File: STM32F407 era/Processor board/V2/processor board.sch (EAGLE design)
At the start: 43 parts, among them IC1 REG1117, U2 MAX13052ESA+, X1 MINI-USB-SCHIELD-32005-201, X2 057-010-1, Y1 25 MHz, Y2 32.768KHz

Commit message: minor updates to board layout
Added USB power fuse, and added toggle switch for boot switch
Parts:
- removed S2: BOOT, SparkFun-Electromechanical:SWITCH-MOMENTARY-2SMD-1101NE
- added U$32: SWITCH_SPDT, SparkFun-Electromechanical:SWITCH_SPDT
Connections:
- new net N$7: C17.P$2, IC1.VIN, PTC1.1
- net 3.3V: now also U$32.O; no longer S2.2
- net N$4: now also U$32.P; no longer S2.1
- net USB_VBUS: now also PTC1.2; no longer C17.P$2, IC1.VIN
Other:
- moved on the sheet: C17, C18, IC1, LED1, PTC1, R3
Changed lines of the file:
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@@
 <part name="U$6" library="microbuilder" deviceset="3.3V" device=""/>
 <part name="S1" library="SparkFun-Electromechanical" deviceset="SWITCH-MOMENTARY-2" device="SMD-1101NE" value="RESET"/>
-<part name="S2" library="SparkFun-Electromechanical" deviceset="SWITCH-MOMENTARY-2" device="SMD-1101NE" value="BOOT"/>
 <part name="R1" library="microbuilder" deviceset="RESISTOR" device="_0603MP" value="500"/>
 <part name="U$7" library="microbuilder" deviceset="3.3V" device=""/>
@@
 <part name="U$12" library="microbuilder" deviceset="GND" device=""/>
 <part name="PTC1" library="microbuilder" deviceset="PTC" device="1206"/>
+<part name="U$32" library="SparkFun-Electromechanical" deviceset="SWITCH_SPDT" device=""/>
 </parts>
 <sheets>
@@
 <instance part="U$6" gate="G$1" x="17.78" y="53.34"/>
 <instance part="S1" gate="G$1" x="162.56" y="10.16"/>
-<instance part="S2" gate="G$1" x="182.88" y="7.62"/>
 <instance part="R1" gate="G$1" x="175.26" y="0" rot="R270"/>
-<instance part="U$7" gate="G$1" x="190.5" y="12.7"/>
+<instance part="U$7" gate="G$1" x="187.96" y="15.24"/>
 <instance part="U$8" gate="G$1" x="175.26" y="-7.62"/>
 <instance part="R2" gate="G$1" x="152.4" y="17.78" rot="R270"/>
@@
 <instance part="BAT1" gate="G$1" x="30.48" y="53.34"/>
 <instance part="U$18" gate="G$1" x="38.1" y="48.26"/>
-<instance part="IC1" gate="G$1" x="251.46" y="104.14"/>
-<instance part="U$19" gate="G$1" x="266.7" y="109.22"/>
-<instance part="U$20" gate="G$1" x="251.46" y="83.82"/>
-<instance part="C17" gate="G$1" x="236.22" y="96.52" rot="R180"/>
-<instance part="C18" gate="G$1" x="266.7" y="96.52"/>
+<instance part="IC1" gate="G$1" x="261.62" y="104.14"/>
+<instance part="U$19" gate="G$1" x="276.86" y="109.22"/>
+<instance part="U$20" gate="G$1" x="261.62" y="83.82"/>
+<instance part="C17" gate="G$1" x="246.38" y="96.52" rot="R180"/>
+<instance part="C18" gate="G$1" x="276.86" y="96.52"/>
 <instance part="U2" gate="A" x="226.06" y="0" smashed="yes">
 <attribute name="NAME" x="221.3356" y="14.1986" size="2.0828" layer="95" ratio="10" rot="SR0"/>
@@
 <instance part="U$30" gate="G$1" x="304.8" y="35.56" rot="MR0"/>
 <instance part="TP1" gate="G$1" x="165.1" y="50.8"/>
-<instance part="LED1" gate="G$1" x="284.48" y="104.14" rot="R90"/>
-<instance part="R3" gate="G$1" x="274.32" y="104.14"/>
-<instance part="U$31" gate="G$1" x="292.1" y="99.06" rot="MR0"/>
+<instance part="LED1" gate="G$1" x="294.64" y="104.14" rot="R90"/>
+<instance part="R3" gate="G$1" x="284.48" y="104.14"/>
+<instance part="U$31" gate="G$1" x="302.26" y="99.06" rot="MR0"/>
 <instance part="JP6" gate="G$1" x="38.1" y="68.58" rot="R180"/>
 <instance part="U$11" gate="G$1" x="215.9" y="25.4" rot="MR0"/>
 <instance part="U$12" gate="G$1" x="203.2" y="25.4" rot="MR0"/>
-<instance part="PTC1" gate="G$1" x="144.78" y="121.92"/>
+<instance part="PTC1" gate="G$1" x="238.76" y="104.14"/>
+<instance part="U$32" gate="G$1" x="180.34" y="7.62"/>
 </instances>
 <busses>
@@
 <pinref part="IC1" gate="G$1" pin="GND"/>
 <pinref part="U$20" gate="G$1" pin="GND"/>
-<wire x1="251.46" y1="86.36" x2="251.46" y2="88.9" width="0.1524" layer="91"/>
+<wire x1="261.62" y1="86.36" x2="261.62" y2="88.9" width="0.1524" layer="91"/>
 <pinref part="C17" gate="G$1" pin="P$1"/>
-<wire x1="251.46" y1="88.9" x2="251.46" y2="91.44" width="0.1524" layer="91"/>
-<wire x1="236.22" y1="91.44" x2="236.22" y2="88.9" width="0.1524" layer="91"/>
-<wire x1="236.22" y1="88.9" x2="251.46" y2="88.9" width="0.1524" layer="91"/>
-<junction x="251.46" y="88.9"/>
+<wire x1="261.62" y1="88.9" x2="261.62" y2="91.44" width="0.1524" layer="91"/>
+<wire x1="246.38" y1="91.44" x2="246.38" y2="88.9" width="0.1524" layer="91"/>
+<wire x1="246.38" y1="88.9" x2="261.62" y2="88.9" width="0.1524" layer="91"/>
+<junction x="261.62" y="88.9"/>
 <pinref part="C18" gate="G$1" pin="P$2"/>
-<wire x1="251.46" y1="88.9" x2="266.7" y2="88.9" width="0.1524" layer="91"/>
-<wire x1="266.7" y1="88.9" x2="266.7" y2="93.98" width="0.1524" layer="91"/>
+<wire x1="261.62" y1="88.9" x2="276.86" y2="88.9" width="0.1524" layer="91"/>
+<wire x1="276.86" y1="88.9" x2="276.86" y2="93.98" width="0.1524" layer="91"/>
 </segment>
 <segment>
@@
 <pinref part="LED1" gate="G$1" pin="C"/>
 <pinref part="U$31" gate="G$1" pin="GND"/>
-<wire x1="289.56" y1="104.14" x2="292.1" y2="104.14" width="0.1524" layer="91"/>
-<wire x1="292.1" y1="104.14" x2="292.1" y2="101.6" width="0.1524" layer="91"/>
+<wire x1="299.72" y1="104.14" x2="302.26" y2="104.14" width="0.1524" layer="91"/>
+<wire x1="302.26" y1="104.14" x2="302.26" y2="101.6" width="0.1524" layer="91"/>
 </segment>
 <segment>
@@
 </segment>
 <segment>
-<pinref part="S2" gate="G$1" pin="2"/>
 <pinref part="U$7" gate="G$1" pin="3.3V"/>
-<wire x1="187.96" y1="7.62" x2="190.5" y2="7.62" width="0.1524" layer="91"/>
-<wire x1="190.5" y1="7.62" x2="190.5" y2="10.16" width="0.1524" layer="91"/>
+<wire x1="185.42" y1="10.16" x2="187.96" y2="10.16" width="0.1524" layer="91"/>
+<wire x1="187.96" y1="10.16" x2="187.96" y2="12.7" width="0.1524" layer="91"/>
+<pinref part="U$32" gate="G$1" pin="O"/>
 </segment>
 <segment>
@@
 <pinref part="IC1" gate="G$1" pin="VOUT"/>
 <pinref part="U$19" gate="G$1" pin="3.3V"/>
-<wire x1="264.16" y1="104.14" x2="266.7" y2="104.14" width="0.1524" layer="91"/>
-<wire x1="266.7" y1="104.14" x2="266.7" y2="106.68" width="0.1524" layer="91"/>
+<wire x1="274.32" y1="104.14" x2="276.86" y2="104.14" width="0.1524" layer="91"/>
+<wire x1="276.86" y1="104.14" x2="276.86" y2="106.68" width="0.1524" layer="91"/>
 <pinref part="C18" gate="G$1" pin="P$1"/>
-<wire x1="266.7" y1="104.14" x2="266.7" y2="101.6" width="0.1524" layer="91"/>
-<junction x="266.7" y="104.14"/>
+<wire x1="276.86" y1="104.14" x2="276.86" y2="101.6" width="0.1524" layer="91"/>
+<junction x="276.86" y="104.14"/>
 <pinref part="R3" gate="G$1" pin="1"/>
-<wire x1="266.7" y1="104.14" x2="269.24" y2="104.14" width="0.1524" layer="91"/>
+<wire x1="276.86" y1="104.14" x2="279.4" y2="104.14" width="0.1524" layer="91"/>
 </segment>
 <segment>
@@
 <segment>
 <pinref part="U1" gate="G$7" pin="BOOT0"/>
-<pinref part="S2" gate="G$1" pin="1"/>
 <wire x1="149.86" y1="7.62" x2="175.26" y2="7.62" width="0.1524" layer="91"/>
 <pinref part="R1" gate="G$1" pin="1"/>
@@
 <wire x1="175.26" y1="7.62" x2="175.26" y2="5.08" width="0.1524" layer="91"/>
 <junction x="175.26" y="7.62"/>
+<pinref part="U$32" gate="G$1" pin="P"/>
 </segment>
 </net>
@@
 <pinref part="C16" gate="G$1" pin="P$1"/>
 <wire x1="213.36" y1="104.14" x2="228.6" y2="104.14" width="0.1524" layer="91"/>
-<pinref part="IC1" gate="G$1" pin="VIN"/>
-<wire x1="228.6" y1="104.14" x2="236.22" y2="104.14" width="0.1524" layer="91"/>
+<pinref part="PTC1" gate="G$1" pin="2"/>
+<wire x1="228.6" y1="104.14" x2="233.68" y2="104.14" width="0.1524" layer="91"/>
 <junction x="228.6" y="104.14"/>
-<pinref part="C17" gate="G$1" pin="P$2"/>
-<wire x1="236.22" y1="104.14" x2="238.76" y2="104.14" width="0.1524" layer="91"/>
-<wire x1="236.22" y1="104.14" x2="236.22" y2="99.06" width="0.1524" layer="91"/>
-<junction x="236.22" y="104.14"/>
 </segment>
 </net>
@@
 <pinref part="R3" gate="G$1" pin="2"/>
 <pinref part="LED1" gate="G$1" pin="A"/>
-<wire x1="281.94" y1="104.14" x2="279.4" y2="104.14" width="0.1524" layer="91"/>
-</segment>
-</net>
+<wire x1="292.1" y1="104.14" x2="289.56" y2="104.14" width="0.1524" layer="91"/>
+</segment>
+</net>
+<net name="N$7" class="0">
+<segment>
+<pinref part="C17" gate="G$1" pin="P$2"/>
+<pinref part="IC1" gate="G$1" pin="VIN"/>
+<wire x1="246.38" y1="104.14" x2="248.92" y2="104.14" width="0.1524" layer="91"/>
+<wire x1="246.38" y1="104.14" x2="246.38" y2="99.06" width="0.1524" layer="91"/>
+<pinref part="PTC1" gate="G$1" pin="1"/>
+<wire x1="243.84" y1="104.14" x2="246.38" y2="104.14" width="0.1524" layer="91"/>
+<junction x="246.38" y="104.14"/>
+</segment>
+</net>

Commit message: fixed CAN controller connections
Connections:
- net CAN_RX: now also U2.RXD; no longer U2.TXD
- net CAN_TX: now also U2.TXD; no longer U2.RXD
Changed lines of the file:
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@@
 <net name="CAN_RX" class="0">
+<segment>
+<wire x1="109.22" y1="111.76" x2="106.68" y2="111.76" width="0.1524" layer="91"/>
+<label x="109.22" y="111.76" size="1.27" layer="95" xref="yes"/>
+<pinref part="U1" gate="G$5" pin="PD0"/>
+</segment>
+<segment>
+<pinref part="U2" gate="A" pin="RXD"/>
+<wire x1="246.38" y1="7.62" x2="243.84" y2="7.62" width="0.1524" layer="91"/>
+<label x="246.38" y="7.62" size="1.27" layer="95" xref="yes"/>
+</segment>
+</net>
+<net name="CAN_TX" class="0">
+<segment>
+<wire x1="109.22" y1="109.22" x2="106.68" y2="109.22" width="0.1524" layer="91"/>
+<label x="109.22" y="109.22" size="1.27" layer="95" xref="yes"/>
+<pinref part="U1" gate="G$5" pin="PD1"/>
+</segment>
 <segment>
 <pinref part="U2" gate="A" pin="TXD"/>
@@
 <label x="205.74" y="2.54" size="1.27" layer="95" rot="R180" xref="yes"/>
 </segment>
-<segment>
-<wire x1="109.22" y1="111.76" x2="106.68" y2="111.76" width="0.1524" layer="91"/>
-<label x="109.22" y="111.76" size="1.27" layer="95" xref="yes"/>
-<pinref part="U1" gate="G$5" pin="PD0"/>
-</segment>
 </net>
-<net name="CAN_TX" class="0">
-<segment>
-<pinref part="U2" gate="A" pin="RXD"/>
-<wire x1="246.38" y1="7.62" x2="243.84" y2="7.62" width="0.1524" layer="91"/>
-<label x="246.38" y="7.62" size="1.27" layer="95" xref="yes"/>
-</segment>
-<segment>
-<wire x1="109.22" y1="109.22" x2="106.68" y2="109.22" width="0.1524" layer="91"/>
-<label x="109.22" y="109.22" size="1.27" layer="95" xref="yes"/>
-<pinref part="U1" gate="G$5" pin="PD1"/>
-</segment>
-</net>

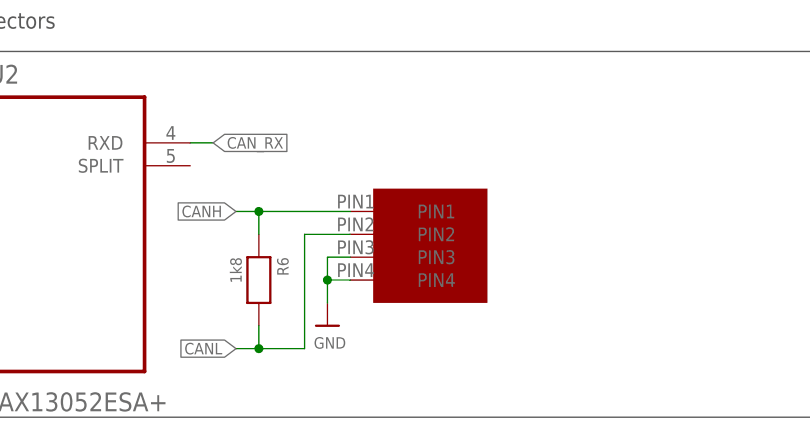
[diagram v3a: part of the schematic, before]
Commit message: minor changes to layout
Fixed impendance circuit for the CAN transciever
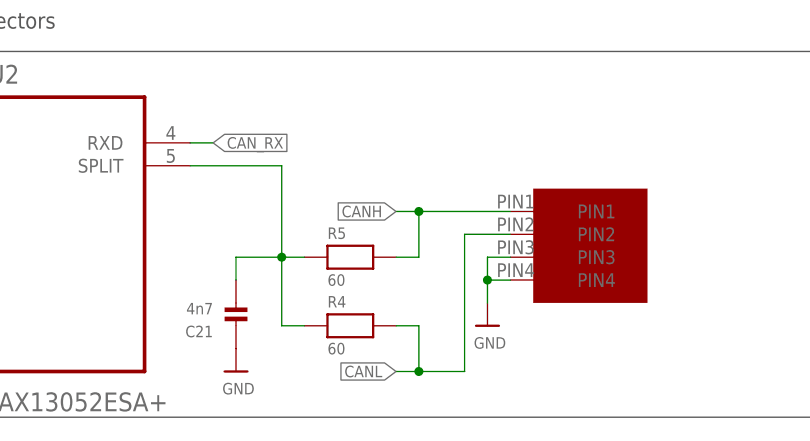
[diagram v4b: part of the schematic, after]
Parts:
- removed R6: 1k8, microbuilder:RESISTOR_0603MP
- added C21: 4n7, microbuilder:CAP_CERAMIC_0603
- added R4, R5: 60, microbuilder:RESISTOR_0603
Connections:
- new net N$8: C21.P$2, R4.1, R5.1, U2.SPLIT
- net CANH: now also R5.2; no longer R6.1
- net CANL: now also R4.2; no longer R6.2
- net GND: now also C21.P$1
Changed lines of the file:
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@@
 <part name="U$23" library="unicorn" deviceset="MICROFIT4" device=""/>
 <part name="U$24" library="microbuilder" deviceset="GND" device=""/>
-<part name="R6" library="microbuilder" deviceset="RESISTOR" device="_0603MP" value="1k8"/>
 <part name="X2" library="con-panduit" deviceset="057-010-" device="1"/>
 <part name="JP1" library="pinhead" deviceset="PINHD-2X11" device=""/>
@@
 <part name="PTC1" library="microbuilder" deviceset="PTC" device="1206"/>
 <part name="U$32" library="SparkFun-Electromechanical" deviceset="SWITCH_SPDT" device=""/>
+<part name="R4" library="microbuilder" deviceset="RESISTOR" device="_0603" value="60"/>
+<part name="R5" library="microbuilder" deviceset="RESISTOR" device="_0603" value="60"/>
+<part name="C21" library="microbuilder" deviceset="CAP_CERAMIC" device="_0603" value="4n7"/>
+<part name="U$33" library="microbuilder" deviceset="GND" device=""/>
 </parts>
 <sheets>
@@
 <instance part="U$21" gate="G$1" x="205.74" y="-15.24"/>
 <instance part="U$22" gate="G$1" x="205.74" y="12.7"/>
-<instance part="U$23" gate="G$1" x="269.24" y="-5.08"/>
-<instance part="U$24" gate="G$1" x="259.08" y="-12.7"/>
-<instance part="R6" gate="G$1" x="251.46" y="-7.62" rot="R270"/>
+<instance part="U$23" gate="G$1" x="287.02" y="-5.08"/>
+<instance part="U$24" gate="G$1" x="276.86" y="-12.7"/>
 <instance part="X2" gate="-1" x="177.8" y="101.6"/>
 <instance part="X2" gate="-2" x="177.8" y="99.06"/>
@@
 <instance part="PTC1" gate="G$1" x="238.76" y="104.14"/>
 <instance part="U$32" gate="G$1" x="180.34" y="7.62"/>
+<instance part="R4" gate="G$1" x="261.62" y="-12.7"/>
+<instance part="R5" gate="G$1" x="261.62" y="-5.08"/>
+<instance part="C21" gate="G$1" x="248.92" y="-10.16" rot="R180"/>
+<instance part="U$33" gate="G$1" x="248.92" y="-17.78"/>
 </instances>
 <busses>
@@
 <pinref part="U$23" gate="G$1" pin="PIN3"/>
 <pinref part="U$24" gate="G$1" pin="GND"/>
-<wire x1="261.62" y1="-5.08" x2="259.08" y2="-5.08" width="0.1524" layer="91"/>
-<wire x1="259.08" y1="-5.08" x2="259.08" y2="-7.62" width="0.1524" layer="91"/>
+<wire x1="279.4" y1="-5.08" x2="276.86" y2="-5.08" width="0.1524" layer="91"/>
+<wire x1="276.86" y1="-5.08" x2="276.86" y2="-7.62" width="0.1524" layer="91"/>
 <pinref part="U$23" gate="G$1" pin="PIN4"/>
-<wire x1="259.08" y1="-7.62" x2="259.08" y2="-10.16" width="0.1524" layer="91"/>
-<wire x1="261.62" y1="-7.62" x2="259.08" y2="-7.62" width="0.1524" layer="91"/>
-<junction x="259.08" y="-7.62"/>
+<wire x1="276.86" y1="-7.62" x2="276.86" y2="-10.16" width="0.1524" layer="91"/>
+<wire x1="279.4" y1="-7.62" x2="276.86" y2="-7.62" width="0.1524" layer="91"/>
+<junction x="276.86" y="-7.62"/>
 </segment>
 <segment>
@@
 <wire x1="213.36" y1="35.56" x2="215.9" y2="35.56" width="0.1524" layer="91"/>
 <wire x1="215.9" y1="35.56" x2="215.9" y2="27.94" width="0.1524" layer="91"/>
+</segment>
+<segment>
+<pinref part="C21" gate="G$1" pin="P$1"/>
+<pinref part="U$33" gate="G$1" pin="GND"/>
 </segment>
 </net>
@@
 <segment>
 <pinref part="U$23" gate="G$1" pin="PIN2"/>
-<wire x1="261.62" y1="-2.54" x2="256.54" y2="-2.54" width="0.1524" layer="91"/>
-<wire x1="256.54" y1="-2.54" x2="256.54" y2="-15.24" width="0.1524" layer="91"/>
-<pinref part="R6" gate="G$1" pin="2"/>
-<wire x1="256.54" y1="-15.24" x2="251.46" y2="-15.24" width="0.1524" layer="91"/>
-<wire x1="251.46" y1="-15.24" x2="251.46" y2="-12.7" width="0.1524" layer="91"/>
-<wire x1="251.46" y1="-15.24" x2="248.92" y2="-15.24" width="0.1524" layer="91"/>
-<junction x="251.46" y="-15.24"/>
-<label x="248.92" y="-15.24" size="1.27" layer="95" rot="R180" xref="yes"/>
+<wire x1="279.4" y1="-2.54" x2="274.32" y2="-2.54" width="0.1524" layer="91"/>
+<wire x1="274.32" y1="-2.54" x2="274.32" y2="-17.78" width="0.1524" layer="91"/>
+<wire x1="274.32" y1="-17.78" x2="269.24" y2="-17.78" width="0.1524" layer="91"/>
+<wire x1="269.24" y1="-17.78" x2="266.7" y2="-17.78" width="0.1524" layer="91"/>
+<junction x="269.24" y="-17.78"/>
+<label x="266.7" y="-17.78" size="1.27" layer="95" rot="R180" xref="yes"/>
+<pinref part="R4" gate="G$1" pin="2"/>
+<wire x1="266.7" y1="-12.7" x2="269.24" y2="-12.7" width="0.1524" layer="91"/>
+<wire x1="269.24" y1="-12.7" x2="269.24" y2="-17.78" width="0.1524" layer="91"/>
 </segment>
 </net>
@@
 <segment>
 <pinref part="U$23" gate="G$1" pin="PIN1"/>
-<pinref part="R6" gate="G$1" pin="1"/>
-<wire x1="261.62" y1="0" x2="251.46" y2="0" width="0.1524" layer="91"/>
-<wire x1="251.46" y1="0" x2="251.46" y2="-2.54" width="0.1524" layer="91"/>
-<wire x1="251.46" y1="0" x2="248.92" y2="0" width="0.1524" layer="91"/>
-<junction x="251.46" y="0"/>
-<label x="248.92" y="0" size="1.27" layer="95" rot="R180" xref="yes"/>
+<wire x1="279.4" y1="0" x2="269.24" y2="0" width="0.1524" layer="91"/>
+<wire x1="269.24" y1="0" x2="266.7" y2="0" width="0.1524" layer="91"/>
+<junction x="269.24" y="0"/>
+<label x="266.7" y="0" size="1.27" layer="95" rot="R180" xref="yes"/>
+<pinref part="R5" gate="G$1" pin="2"/>
+<wire x1="266.7" y1="-5.08" x2="269.24" y2="-5.08" width="0.1524" layer="91"/>
+<wire x1="269.24" y1="-5.08" x2="269.24" y2="0" width="0.1524" layer="91"/>
 </segment>
 </net>
@@
 </segment>
 </net>
+<net name="N$8" class="0">
+<segment>
+<pinref part="R4" gate="G$1" pin="1"/>
+<wire x1="256.54" y1="-12.7" x2="254" y2="-12.7" width="0.1524" layer="91"/>
+<wire x1="254" y1="-12.7" x2="254" y2="-5.08" width="0.1524" layer="91"/>
+<pinref part="R5" gate="G$1" pin="1"/>
+<wire x1="254" y1="-5.08" x2="256.54" y2="-5.08" width="0.1524" layer="91"/>
+<wire x1="254" y1="-5.08" x2="254" y2="5.08" width="0.1524" layer="91"/>
+<junction x="254" y="-5.08"/>
+<pinref part="U2" gate="A" pin="SPLIT"/>
+<wire x1="254" y1="5.08" x2="243.84" y2="5.08" width="0.1524" layer="91"/>
+<pinref part="C21" gate="G$1" pin="P$2"/>
+<wire x1="254" y1="-5.08" x2="248.92" y2="-5.08" width="0.1524" layer="91"/>
+<wire x1="248.92" y1="-5.08" x2="248.92" y2="-7.62" width="0.1524" layer="91"/>
+</segment>
+</net>
